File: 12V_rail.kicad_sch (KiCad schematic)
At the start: 3 parts, among them J1 39-30-0080

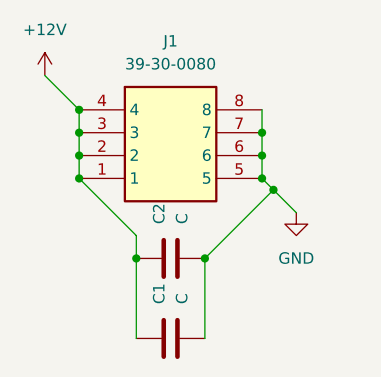
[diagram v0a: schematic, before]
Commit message: feat: add Mol connectors and update schematic and PCB designs
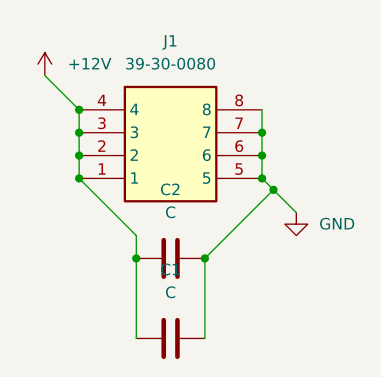
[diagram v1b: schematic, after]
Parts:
- C1, C2: footprint Capacitor_SMD:C_1206_3216Metric_Pad1.33x1.80mm_HandSolder -> (none)
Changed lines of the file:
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@@
 		(fields_autoplaced yes)
 		(property "Reference" "C2"
-			(at 49.5299 50.8 0)
-			(show_name no)
-			(do_not_autoplace no)
-			(effects
-				(font
-					(size 1.27 1.27)
-				)
-				(justify left)
+			(at 50.8 46.99 90)
+			(show_name no)
+			(do_not_autoplace no)
+			(effects
+				(font
+					(size 1.27 1.27)
+				)
 			)
 		)
 		(property "Value" "C"
-			(at 52.0699 50.8 0)
-			(show_name no)
-			(do_not_autoplace no)
-			(effects
-				(font
-					(size 1.27 1.27)
-				)
-				(justify left)
-			)
-		)
-		(property "Footprint" "Capacitor_SMD:C_1206_3216Metric_Pad1.33x1.80mm_HandSolder"
+			(at 50.8 49.53 90)
+			(show_name no)
+			(do_not_autoplace no)
+			(effects
+				(font
+					(size 1.27 1.27)
+				)
+			)
+		)
+		(property "Footprint" ""
 			(at 54.61 53.6448 0)
 			(hide yes)
@@
 		)
 		(property "Value" "+12V"
-			(at 36.83 29.21 0)
-			(show_name no)
-			(do_not_autoplace no)
-			(effects
-				(font
-					(size 1.27 1.27)
-				)
+			(at 39.37 33.0199 0)
+			(show_name no)
+			(do_not_autoplace no)
+			(effects
+				(font
+					(size 1.27 1.27)
+				)
+				(justify left)
 			)
 		)
@@
 		)
 		(property "Value" "GND"
-			(at 64.77 54.61 0)
-			(show_name no)
-			(do_not_autoplace no)
-			(effects
-				(font
-					(size 1.27 1.27)
-				)
+			(at 67.31 50.7999 0)
+			(show_name no)
+			(do_not_autoplace no)
+			(effects
+				(font
+					(size 1.27 1.27)
+				)
+				(justify left)
 			)
 		)
@@
 		(fields_autoplaced yes)
 		(property "Reference" "C1"
-			(at 49.5299 59.69 0)
-			(show_name no)
-			(do_not_autoplace no)
-			(effects
-				(font
-					(size 1.27 1.27)
-				)
-				(justify left)
+			(at 50.8 55.88 90)
+			(show_name no)
+			(do_not_autoplace no)
+			(effects
+				(font
+					(size 1.27 1.27)
+				)
 			)
 		)
 		(property "Value" "C"
-			(at 52.0699 59.69 0)
-			(show_name no)
-			(do_not_autoplace no)
-			(effects
-				(font
-					(size 1.27 1.27)
-				)
-				(justify left)
-			)
-		)
-		(property "Footprint" "Capacitor_SMD:C_1206_3216Metric_Pad1.33x1.80mm_HandSolder"
+			(at 50.8 58.42 90)
+			(show_name no)
+			(do_not_autoplace no)
+			(effects
+				(font
+					(size 1.27 1.27)
+				)
+			)
+		)
+		(property "Footprint" ""
 			(at 54.61 62.5348 0)
 			(hide yes)
